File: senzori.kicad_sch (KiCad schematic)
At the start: 21 parts, among them Q3 NPN, Q4 NPN, U300 TMP117xxDRV, U301 MS5611-01BA, U302 L96-M33, U303 BME680

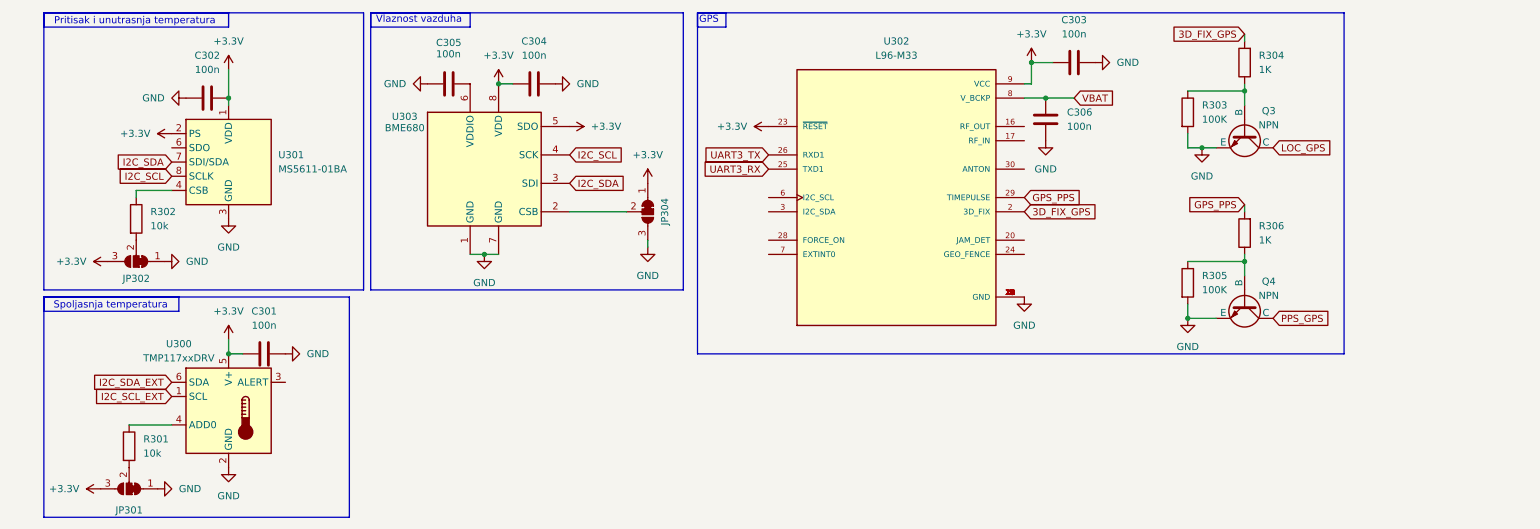
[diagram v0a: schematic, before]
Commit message: Znacajne izmene seme
Dodao prikljucak za UV senzor
Dodao reset za GPS
Dodao ext_ant za GPS
Dodao 3D modele
Dodao testpoint-e
Sredio semu malo
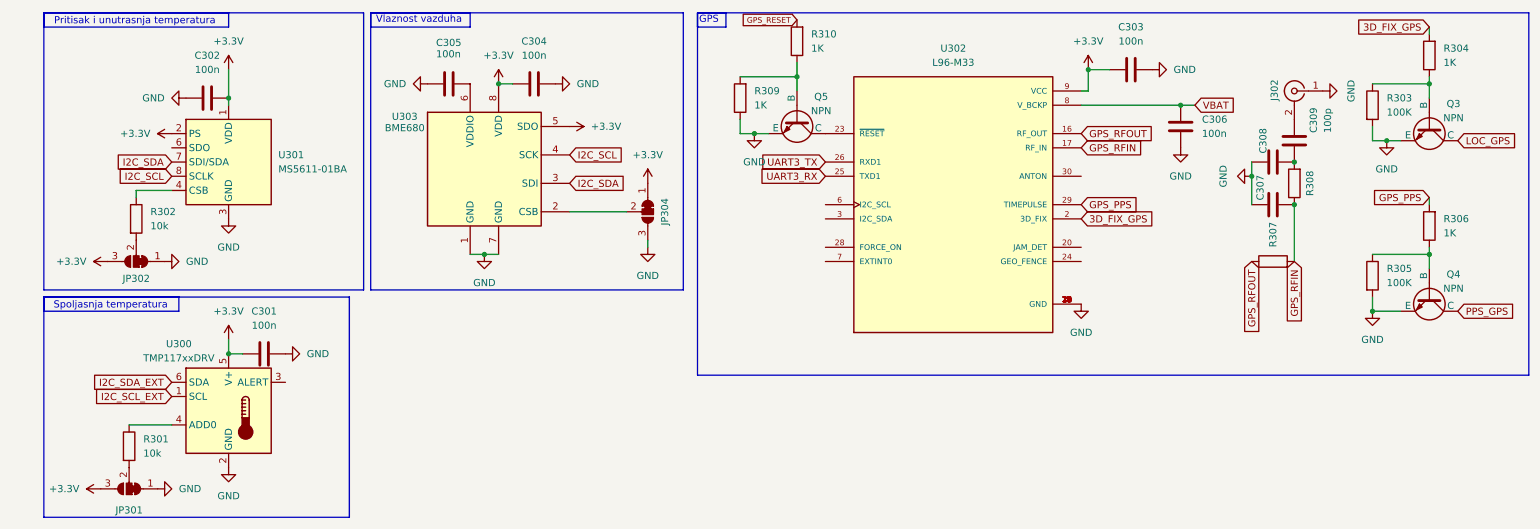
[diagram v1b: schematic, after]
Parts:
- added C307, C308: 0, Capacitor_SMD:C_1206_3216Metric_Pad1.33x1.80mm_HandSolder, symbol Device:C
- added C309: 100p, Capacitor_SMD:C_1206_3216Metric_Pad1.33x1.80mm_HandSolder, symbol Device:C
- added J302: ~, Connector_Coaxial:SMA_Amphenol_132134-16_Vertical, symbol Connector:Conn_Coaxial
- added Q5: NPN, Package_TO_SOT_SMD:TSOT-23_HandSoldering, symbol Simulation_SPICE:NPN
- added R307, R308: 0, Resistor_SMD:R_1206_3216Metric_Pad1.30x1.75mm_HandSolder, symbol Device:R
- added R309, R310: 1K, Resistor_SMD:R_1206_3216Metric_Pad1.30x1.75mm_HandSolder, symbol Device:R
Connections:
- net +3.3V: no longer U302.23 (~{RESET})
- net GND: now also C307.1, C308.1, J302.1 (In), Q5.3 (E), R309.1
- net GPS_RFOUT: now reaches U302.16 (RF_OUT)
- net GPS_RFOUT: now also R307.1
- net GPS_RFIN: now reaches U302.17 (RF_IN)
- net GPS_RFIN: now also C307.2, R307.2, R308.1
- new net: C309.1, J302.2 (Ext)
- new net: C308.2, C309.2, R308.2
- new net: Q5.2 (B), R309.2, R310.1
- new net: Q5.1 (C), U302.23 (~{RESET})
- new net GPS_RESET: R310.2
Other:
- moved on the sheet: C303, C306, Q3, Q4, R303, R304, R305, R306, U302

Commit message: Layout i rutiranje za EXT PCB uradjeni
Uradio sam layout i rutiranje za plocicu sa sijalicama i senzorom temperature koja ce biti montirana napolju
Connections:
- net +3.3V: no longer C301.1, JP301.3 (B), U300.5 (V+)
- net GND: no longer C301.2, JP301.1 (A), U300.2 (GND)
- new net EXR_+3.3V: C301.1, JP301.3 (B), U300.5 (V+)
- new net EXT_GND: C301.2, JP301.1 (A), U300.2 (GND)
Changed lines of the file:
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@@
 			)
 		)
-		(property "Value" "GND"
+		(property "Value" "EXT_GND"
 			(at 48.26 101.6 0)
 			(effects
@@
 			)
 		)
-		(property "Value" "GND"
+		(property "Value" "EXT_GND"
 			(at 39.37 100.3299 90)
 			(effects
@@
 			)
 		)
-		(property "Value" "+3.3V"
+		(property "Value" "EXR_+3.3V"
 			(at 48.26 68.58 0)
 			(effects
@@
 			)
 		)
-		(property "Value" "+3.3V"
+		(property "Value" "EXR_+3.3V"
 			(at 21.59 100.3299 90)
 			(effects
@@
 			)
 		)
-		(property "Value" "GND"
+		(property "Value" "EXT_GND"
 			(at 62.23 76.1999 90)
 			(effects

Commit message: Manje izmene seme
Sredio izgled seme
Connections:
- net EXR_+3.3V renamed EXT_+3.3V
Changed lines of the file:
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@@
 	(wire
 		(pts
+			(xy 48.26 97.79) (xy 48.26 96.52)
+		)
+		(stroke
+			(width 0)
+			(type default)
+		)
+	)
+	(wire
+		(pts
 			(xy 262.89 27.94) (xy 262.89 26.67)
 		)
@@
 	(symbol
 		(lib_id "power:GND")
-		(at 48.26 96.52 0)
+		(at 48.26 97.79 0)
 		(unit 1)
 		(exclude_from_sim no)
@@
 		(fields_autoplaced yes)
 		(property "Reference" "#PWR035"
-			(at 48.26 102.87 0)
+			(at 48.26 104.14 0)
 			(effects
 				(font
@@
 		)
 		(property "Value" "EXT_GND"
-			(at 48.26 101.6 0)
+			(at 48.26 102.87 0)
 			(effects
 				(font
@@
 		)
 		(property "Footprint" ""
-			(at 48.26 96.52 0)
+			(at 48.26 97.79 0)
 			(effects
 				(font
@@
 		)
 		(property "Datasheet" ""
-			(at 48.26 96.52 0)
+			(at 48.26 97.79 0)
 			(effects
 				(font
@@
 		)
 		(property "Description" "Power symbol creates a global label with name \"GND\" , ground"
-			(at 48.26 96.52 0)
+			(at 48.26 97.79 0)
 			(effects
 				(font
@@
 		(on_board yes)
 		(dnp no)
-		(fields_autoplaced yes)
 		(property "Reference" "#PWR033"
 			(at 41.91 100.33 0)
@@
 		)
 		(property "Value" "EXT_GND"
-			(at 39.37 100.3299 90)
+			(at 36.83 98.552 90)
 			(effects
 				(font
@@
 		(on_board yes)
 		(dnp no)
-		(fields_autoplaced yes)
 		(property "Reference" "#PWR034"
 			(at 48.26 77.47 0)
@@
 			)
 		)
-		(property "Value" "EXR_+3.3V"
-			(at 48.26 68.58 0)
+		(property "Value" "EXT_+3.3V"
+			(at 45.974 69.088 0)
 			(effects
 				(font
@@
 		(on_board yes)
 		(dnp no)
-		(fields_autoplaced yes)
 		(property "Reference" "#PWR032"
 			(at 29.21 100.33 0)
@@
 			)
 		)
-		(property "Value" "EXR_+3.3V"
-			(at 21.59 100.3299 90)
+		(property "Value" "EXT_+3.3V"
+			(at 26.162 98.044 90)
 			(effects
 				(font
@@
 		(on_board yes)
 		(dnp no)
-		(fields_autoplaced yes)
 		(property "Reference" "#PWR058"
 			(at 64.77 76.2 0)
@@
 		)
 		(property "Value" "EXT_GND"
-			(at 62.23 76.1999 90)
+			(at 61.214 75.946 90)
 			(effects
 				(font

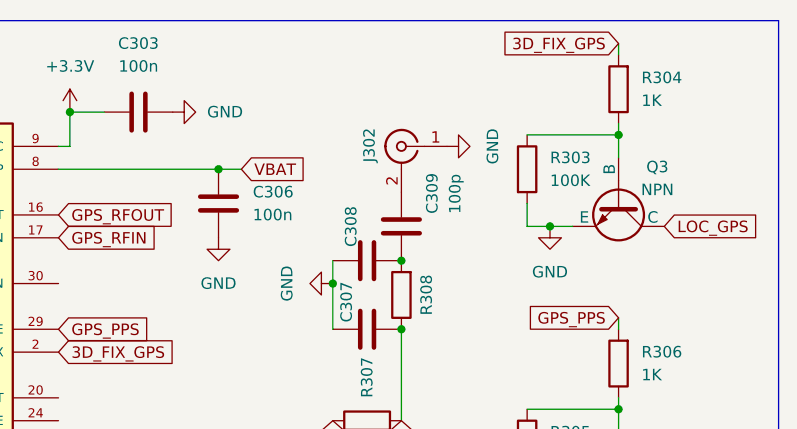
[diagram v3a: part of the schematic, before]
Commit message: Znacajne izmene seme i pcb-a
Napravljen nov layout
dodat konektor za gpio
dodat konektor za eksterna merenja vetra
izmenjene diag lampice
izmenjen konektor za ext plocu
razno
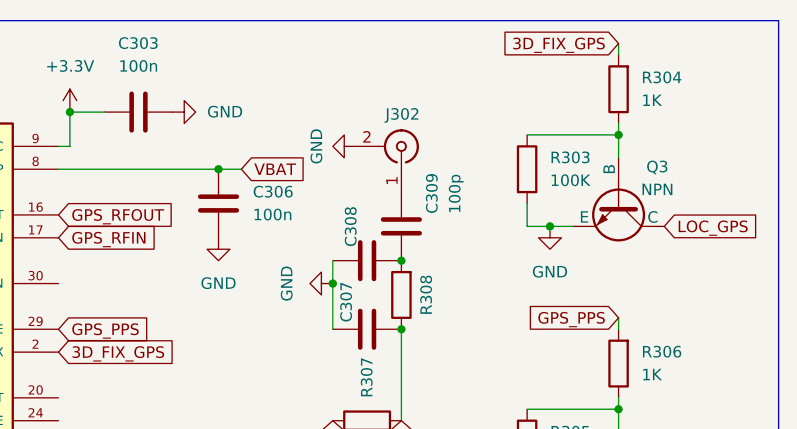
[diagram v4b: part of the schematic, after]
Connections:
- net GND: now also J302.2 (Ext); no longer J302.1 (In)
- net at C309.1: now also J302.1 (In); no longer J302.2 (Ext)
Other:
- moved on the sheet: J302
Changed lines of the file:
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@@
 	(symbol
 		(lib_id "Connector:Conn_Coaxial")
-		(at 238.76 29.21 0)
-		(mirror y)
+		(at 238.76 29.21 270)
+		(mirror x)
 		(unit 1)
 		(exclude_from_sim no)
@@
 		(dnp no)
 		(property "Reference" "J302"
-			(at 235.204 30.988 90)
+			(at 236.982 25.654 90)
 			(effects
 				(font
@@
 		)
 		(property "Value" "~"
-			(at 237.8075 25.4 90)
+			(at 242.57 28.2575 90)
 			(effects
 				(font
@@
 	(symbol
 		(lib_id "power:GND")
-		(at 243.84 29.21 90)
+		(at 233.68 29.21 270)
 		(unit 1)
 		(exclude_from_sim no)
@@
 		(dnp no)
 		(property "Reference" "#PWR087"
-			(at 250.19 29.21 0)
+			(at 227.33 29.21 0)
 			(effects
 				(font
@@
 		)
 		(property "Value" "GND"
-			(at 248.92 29.21 0)
+			(at 229.362 29.21 0)
 			(effects
 				(font
@@
 		)
 		(property "Footprint" ""
-			(at 243.84 29.21 0)
+			(at 233.68 29.21 0)
 			(effects
 				(font
@@
 		)
 		(property "Datasheet" ""
-			(at 243.84 29.21 0)
+			(at 233.68 29.21 0)
 			(effects
 				(font
@@
 		)
 		(property "Description" "Power symbol creates a global label with name \"GND\" , ground"
-			(at 243.84 29.21 0)
+			(at 233.68 29.21 0)
 			(effects
 				(font
